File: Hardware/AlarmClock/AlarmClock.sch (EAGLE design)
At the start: 9 parts, among them CN1 Speaker, IC1 ATMEGA2560-16AU, IC2 DS3231/SO, IC3 CAT24C32WI-GT3, J1 LCD, SW1 SKQGADE010, U1 TEMT6000X01

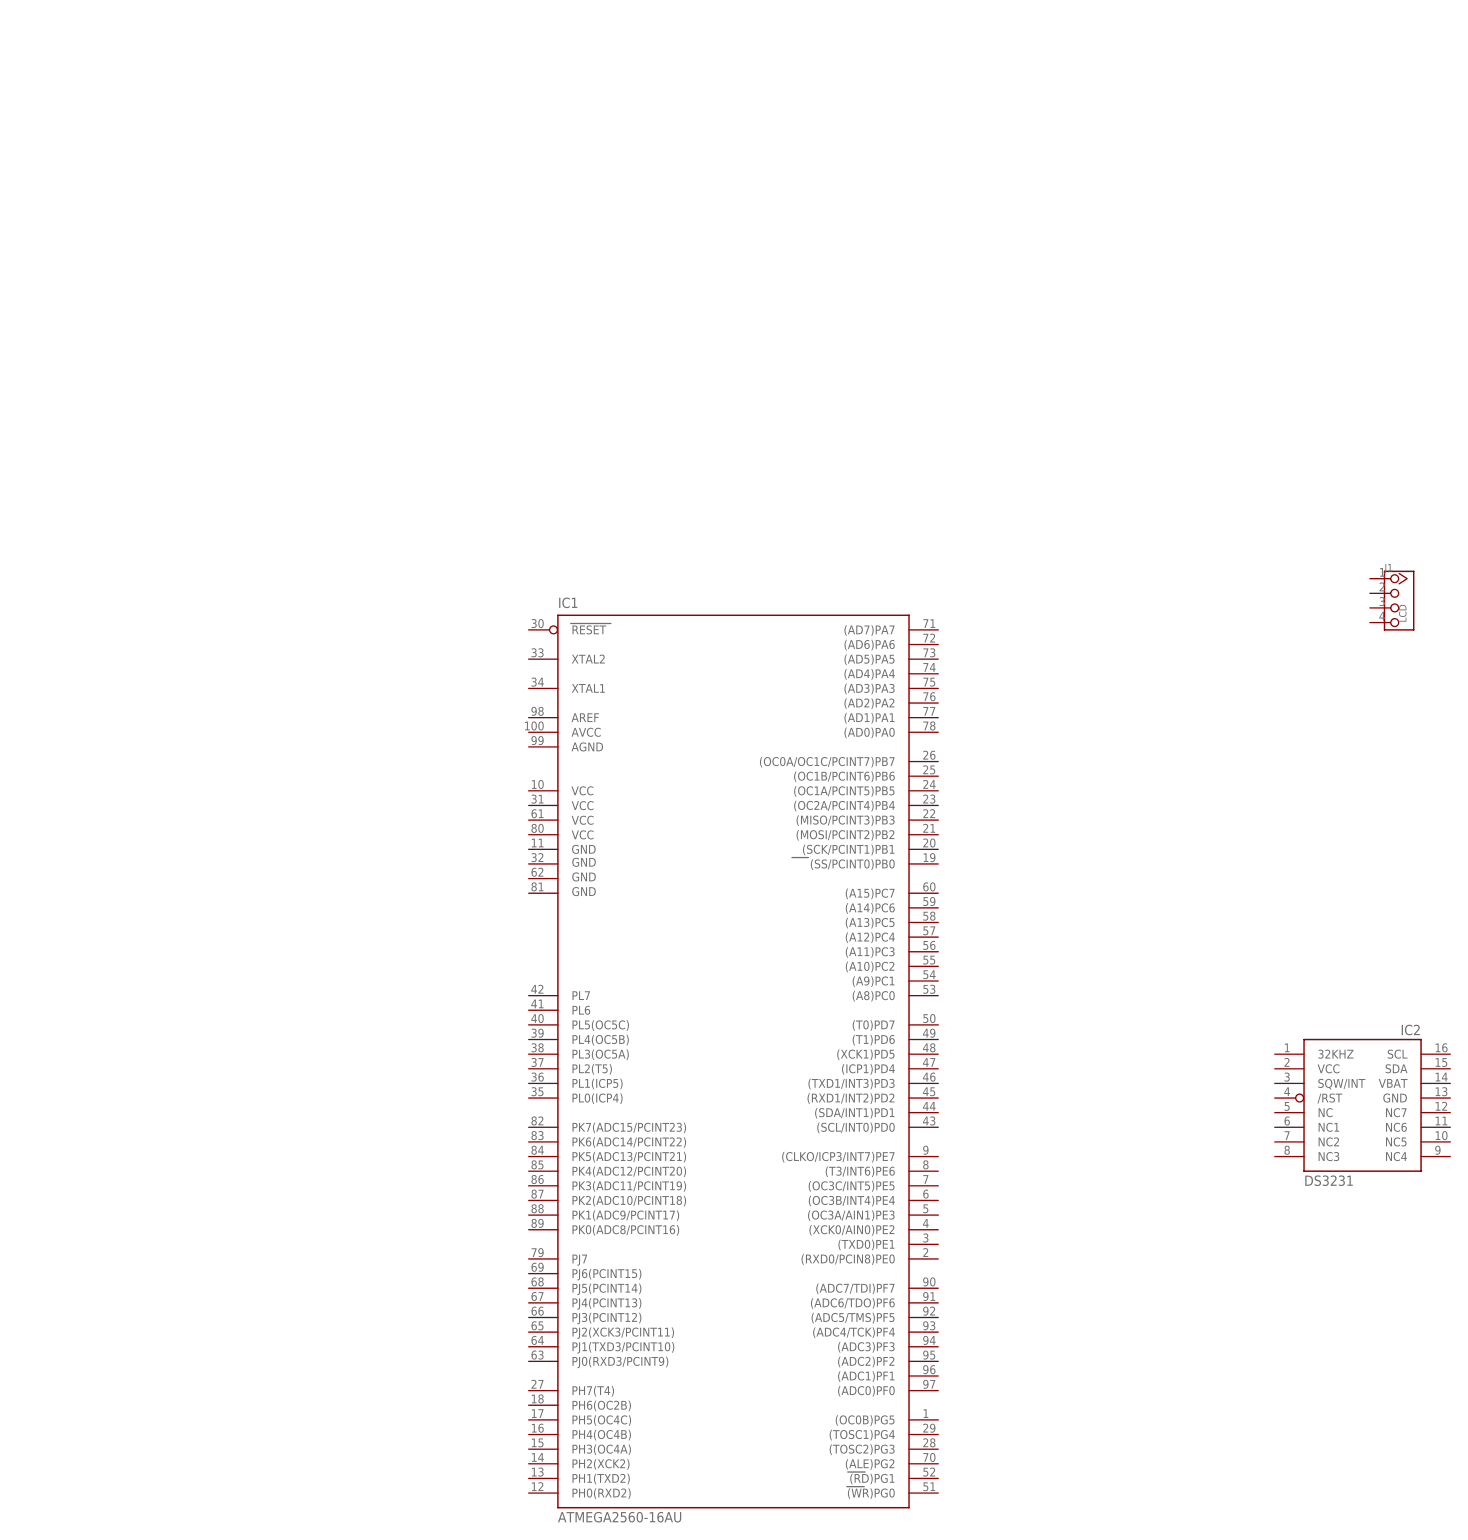
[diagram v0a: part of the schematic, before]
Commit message: add pwr and jtag
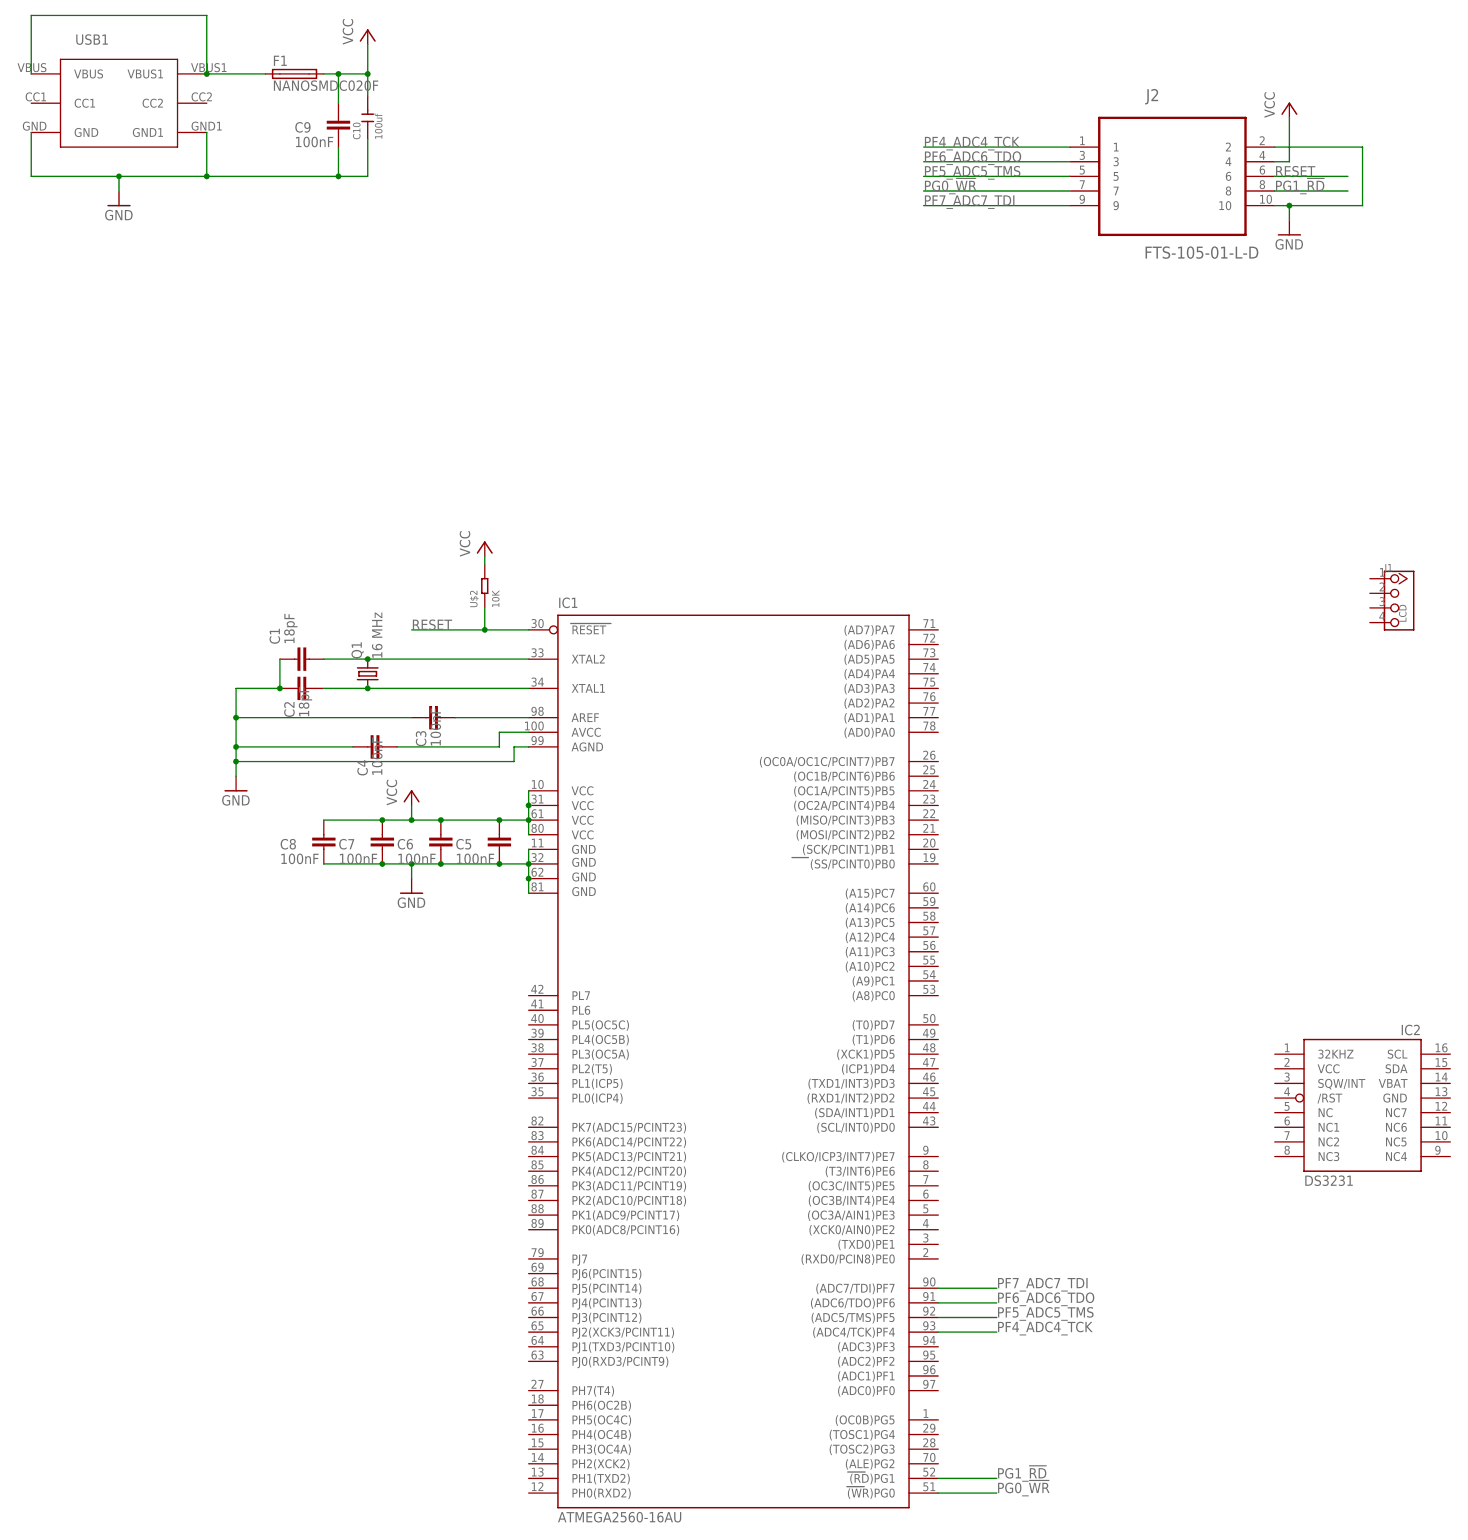
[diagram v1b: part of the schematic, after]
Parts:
- added C1, C2: 18pF, Capacitor:C_CHIP-0805(2012-METRIC)
- added C10: 100uf, OPL_Capacitor:CERAMIC-100UF-6.3V-20%-X5R(1206)
- added C3, C4, C5, C6, C7, C8, C9: 100nF, Capacitor:C_CHIP-0805(2012-METRIC)
- added F1: NANOSMDC020F, Circuit-Protection:FUSE_NANOSMDC020F-2_CHIP-1206
- added J2: FTS-105-01-L-D, JTAG_10pol_50mil-MSW193:FTS-105-01-L-D
- added Q1: 16 MHz, adafruit:CRYSTALHC49UP
- added U$2: 10K, OPL_Resistor:SMD-RES-10K-1%-1/8W(0805)
- added USB1: USB_TYPE_C, Usb_c:USB_TYPE_C
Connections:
- new net GND: C1.1, C10.1, C2.1, C3.1, C4.1, C5.2, C6.2, C7.2, C8.2, C9.2, IC1.AGND, IC1.GND, IC1.GND1, IC1.GND2, IC1.GND3, J2.10, J2.2, USB1.GND, USB1.GND1
- new net N$4: C2.2, IC1.XTAL1, Q1.1
- new net N$5: C1.2, IC1.XTAL2, Q1.2
- new net N$6: C4.2, IC1.AVCC
- new net N$7: C3.2, IC1.AREF
- new net N$8: F1.1, USB1.VBUS, USB1.VBUS1
- new net PF4_ADC4_TCK: IC1.(ADC4/TCK)PF4, J2.1
- new net PF5_ADC5_TMS: IC1.(ADC5/TMS)PF5, J2.5
- new net PF6_ADC6_TDO: IC1.(ADC6/TDO)PF6, J2.3
- new net PF7_ADC7_TDI: IC1.(ADC7/TDI)PF7, J2.9
- new net PG0_!WR: IC1.(WR)PG0, J2.7
- new net PG1_!RD: IC1.(RD)PG1, J2.8
- new net RESET: IC1.RESET, J2.6, U$2.1
- new net VCC: C10.2, C5.1, C6.1, C7.1, C8.1, C9.1, F1.2, IC1.VCC, IC1.VCC1, IC1.VCC2, IC1.VCC3, J2.4, U$2.2
